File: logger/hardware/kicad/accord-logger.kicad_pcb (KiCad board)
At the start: 2 copper layers, 120 x 80 mm, 37 parts, among them J1 Board connector 14-way, J5 SD breakout 6-way, Q5 IPD50P04P4L-11, Q6 2N3904, Q7 2N3904, U1 RaspberryPi_Pico_W, U16 DS3231SN, U6 LM2678T-5.0

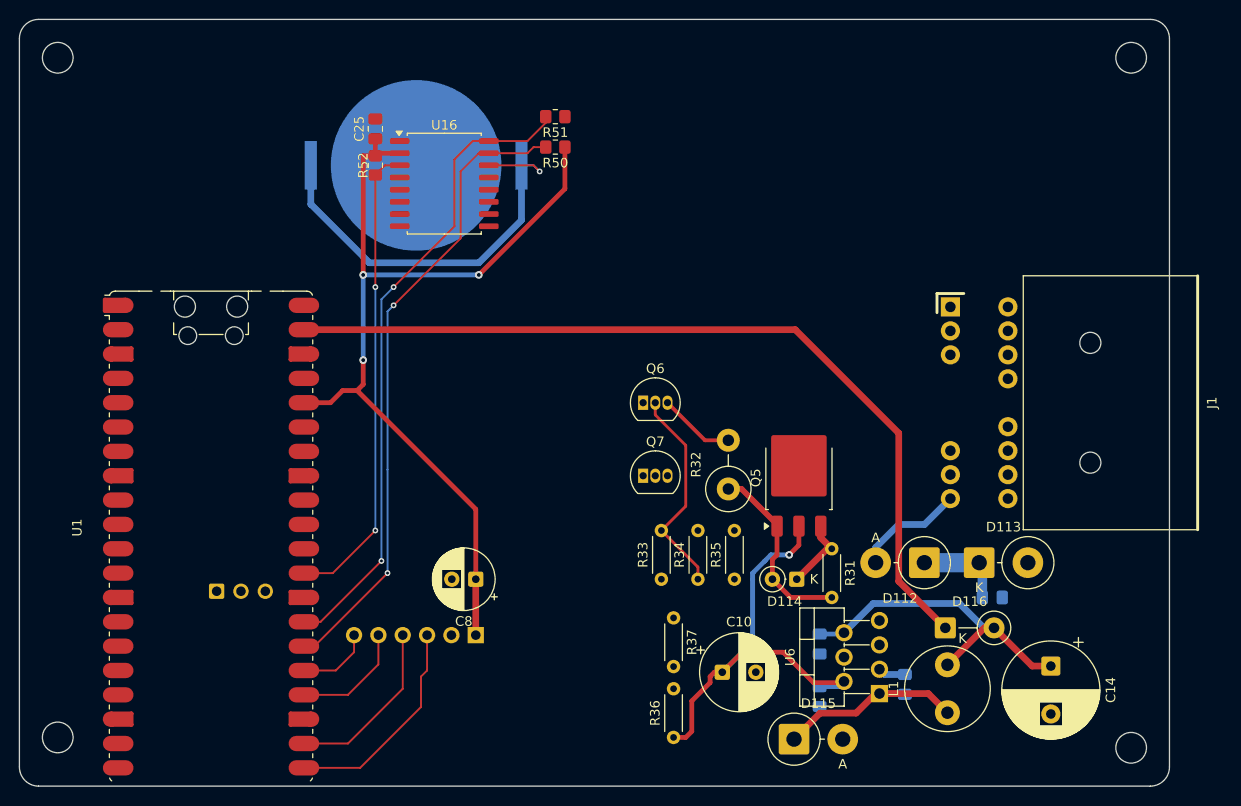
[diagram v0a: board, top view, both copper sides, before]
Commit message: layout: PGND pour on both layers; P12 and VIN_SW fixed
Owner revisions after review: P12 joined from D112 to Q5 pin 3
(15.8 mm); VIN_SW now lands on Q5's tab, not the middle lead; one PGND
zone on F.Cu and B.Cu, filled as a single island per layer, which joins
all 35 open ground connections. The Pico footprint's antenna and RF
keepouts already exclude it; the wider "suggestion" strip is to be cut
out later.

Open (scratch DRC, parity 0): starved thermal on U6 pin 4; C11 ground
pad reaches U6 pin 4 only through the back pour, around a VIN_SW stub;
unrouted R51.1 (3V3), R37.1 (B5), Q7.2-R35 (HOLD_B), U1.33-J1.10 (AGND,
with the inputs).

Claude-Session-ID: 42dd0e33-28b5-4936-847e-9c2e1d2488fa
Co-Authored-By: Claude Opus 5.5 <noreply@anthropic.com>
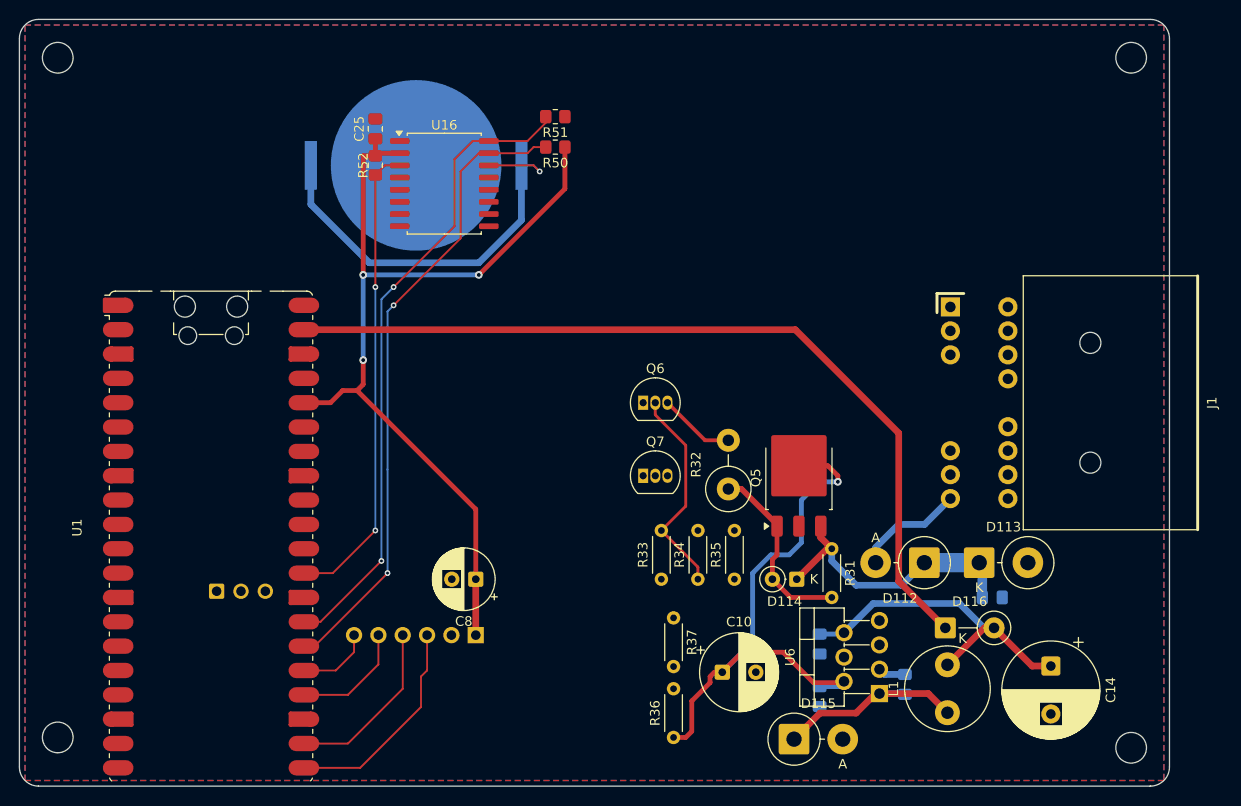
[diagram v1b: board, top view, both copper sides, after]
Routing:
- net /P12: track 17.3 -> 30.3 mm
- net /VIN_SW: track 47.5 -> 60.1 mm
- added copper zone on B.Cu, net /PGND
- added copper zone on F.Cu, net /PGND
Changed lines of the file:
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@@
+	)
+	(segment
+		(start 175.895 118.745)
+		(end 180.655 118.745)
+		(width 0.7)
+		(layer "B.Cu")
+		(net 6)
+	)
+	(segment
+		(start 173.355 114.935)
+		(end 173.355 116.205)
+		(width 0.7)
+		(layer "B.Cu")
+		(net 6)
+	)
+	(segment
+		(start 173.355 116.205)
+		(end 175.895 118.745)
+		(width 0.7)
+		(layer "B.Cu")
+		(net 6)
 	)
 	(segment
@@
 	)
 	(segment
+		(start 180.655 118.745)
+		(end 183.015 116.385)
+		(width 0.7)
+		(layer "B.Cu")
+		(net 6)
+	)
+	(segment
 		(start 183.015 116.385)
 		(end 188.735 116.385)
@@
 	)
 	(segment
-		(start 168.91 115.57)
-		(end 169.925 114.555)
+		(start 173.99 107.315)
+		(end 172.95 106.275)
 		(width 0.5)
 		(layer "F.Cu")
@@
 	)
 	(segment
+		(start 172.95 106.275)
+		(end 169.925 106.275)
+		(width 0.5)
+		(layer "F.Cu")
+		(net 7)
+	)
+	(segment
 		(start 168.275 125.73)
 		(end 171.45 128.905)
@@
 	)
 	(segment
-		(start 169.925 114.555)
-		(end 169.925 112.575)
-		(width 0.5)
-		(layer "F.Cu")
-		(net 7)
-	)
-	(segment
 		(start 158.75 133.985)
 		(end 158.75 130.81)
@@
 	)
 	(segment
+		(start 173.99 107.95)
+		(end 173.99 107.315)
+		(width 0.5)
+		(layer "F.Cu")
+		(net 7)
+	)
+	(segment
 		(start 171.45 128.905)
 		(end 174.499823 128.905)
@@
 	)
 	(via
-		(at 168.91 115.57)
+		(at 173.99 107.95)
 		(size 0.8)
 		(drill 0.4)
@@
 	)
 	(segment
+		(start 172.085 107.95)
+		(end 170.18 109.855)
+		(width 0.5)
+		(layer "B.Cu")
+		(net 7)
+	)
+	(segment
+		(start 165.1 124.645)
+		(end 161.93 127.815)
+		(width 0.5)
+		(layer "B.Cu")
+		(net 7)
+	)
+	(segment
+		(start 170.18 114.3)
+		(end 168.91 115.57)
+		(width 0.5)
+		(layer "B.Cu")
+		(net 7)
+	)
+	(segment
 		(start 167.005 115.57)
-		(end 168.91 115.57)
-		(width 0.5)
-		(layer "B.Cu")
-		(net 7)
-	)
-	(segment
-		(start 161.93 127.815)
-		(end 165.1 124.645)
+		(end 165.1 117.475)
 		(width 0.5)
 		(layer "B.Cu")
@@
 	)
 	(segment
+		(start 168.91 115.57)
+		(end 167.005 115.57)
+		(width 0.5)
+		(layer "B.Cu")
+		(net 7)
+	)
+	(segment
+		(start 173.99 107.95)
+		(end 172.085 107.95)
+		(width 0.5)
+		(layer "B.Cu")
+		(net 7)
+	)
+	(segment
+		(start 170.18 109.855)
+		(end 170.18 114.3)
+		(width 0.5)
+		(layer "B.Cu")
+		(net 7)
+	)
+	(segment
 		(start 174.087323 129.3175)
 		(end 174.63 128.774823)
@@
 	)
 	(segment
-		(start 166.37 116.205)
-		(end 167.005 115.57)
-		(width 0.5)
-		(layer "B.Cu")
-		(net 7)
-	)
-	(segment
-		(start 165.1 124.645)
-		(end 165.1 118.11)
-		(width 0.5)
-		(layer "B.Cu")
-		(net 7)
-	)
-	(segment
-		(start 165.1 118.11)
-		(end 165.1 117.475)
-		(width 0.5)
-		(layer "B.Cu")
-		(net 7)
-	)
-	(segment
 		(start 165.1 117.475)
-		(end 166.37 116.205)
+		(end 165.1 124.645)
 		(width 0.5)
 		(layer "B.Cu")
@@
 		(net 59)
 	)
+	(zone
+		(net 4)
+		(net_name "/PGND")
+		(layers "F.Cu" "B.Cu")
+		(hatch edge 0.5)
+		(connect_pads
+			(clearance 0.5)
+		)
+		(min_thickness 0.25)
+		(filled_areas_thickness no)
+		(fill yes
+			(thermal_gap 0.5)
+			(thermal_bridge_width 0.5)
+		)
+		(polygon
+			(pts
+				(xy 89.175787 60.285786) (xy 208.004214 60.285786) (xy 208.004214 139.114214) (xy 89.175787 139.114214)
+			)
+		)
+	)
 	(embedded_fonts no)

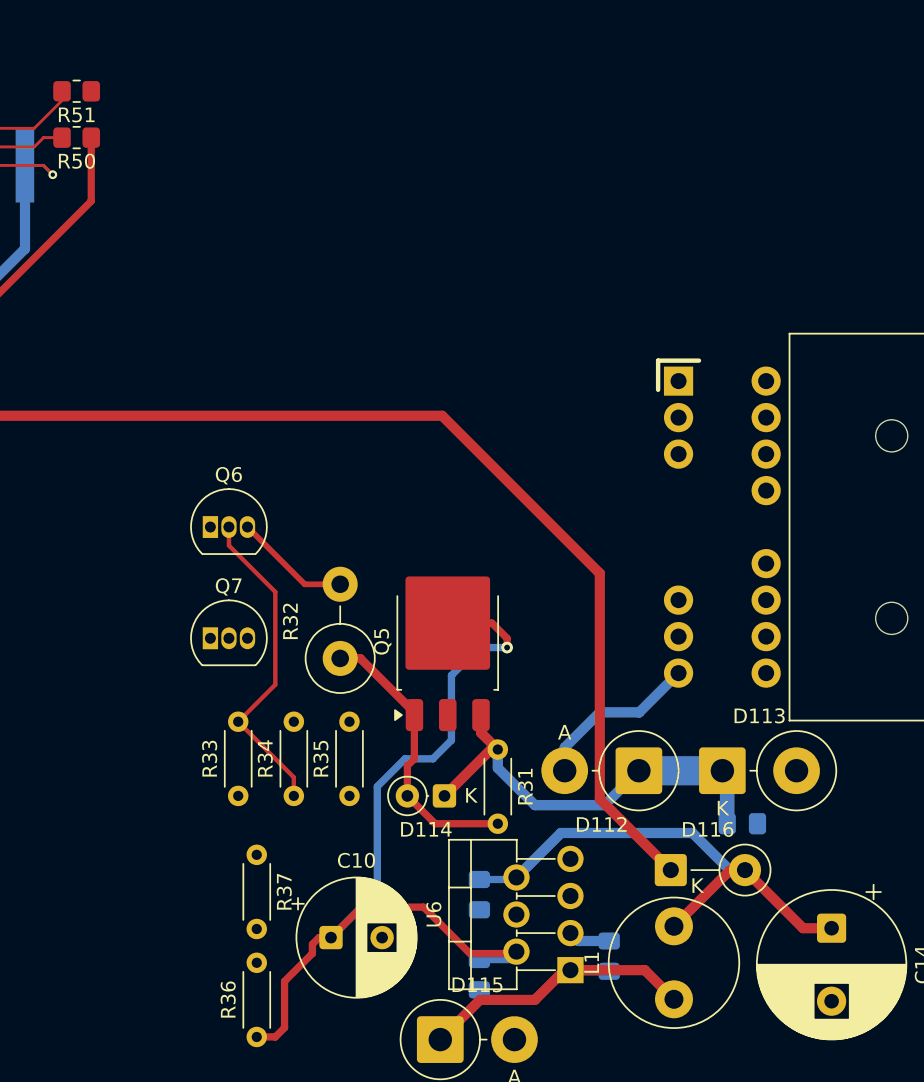
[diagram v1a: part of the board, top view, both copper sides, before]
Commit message: layout: remaining power-block connections routed
R51 pin 1 to 3V3 (3.2 mm to R50), Q7 base to R35 (HOLD_B, 15 mm,
0.2 mm B.Cu), R37 to B5; B5 rerouted at 0.5 mm; PGND tracks added at U6
pin 4 and C11 (C11 ground to U6.4 now 12.3 mm by track, plus the pour).

Saved with the PGND zone unfilled. Refilled in a scratch copy with the
pcbnew zone filler: one island per layer; DRC schematic parity 0, no
clearance, courtyard or thermal errors (the U6 pin 4 starved thermal is
gone); unconnected only U1.33-J1.10 (AGND, comes with the inputs) and
Q5's middle-lead pad (joined to the tab inside the part).

Claude-Session-ID: 42dd0e33-28b5-4936-847e-9c2e1d2488fa
Co-Authored-By: Claude Opus 5.5 <noreply@anthropic.com>
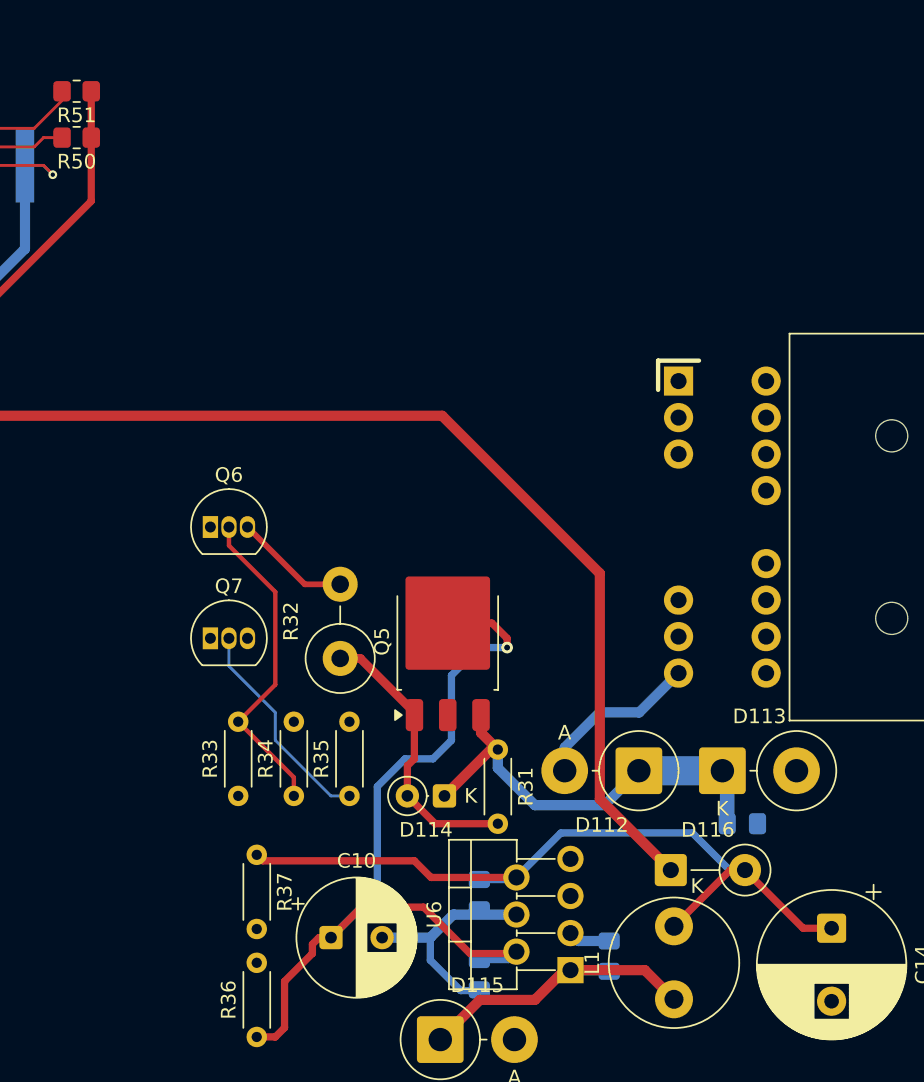
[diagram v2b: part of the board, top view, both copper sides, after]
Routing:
- net /B5: track 34.6 -> 53.0 mm
- net /PGND: track 0.00 -> 15.6 mm
- net /HOLD_B: track 0.00 -> 15.0 mm
- net /P3V3_SW: track 96.3 -> 99.5 mm
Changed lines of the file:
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@@
+	)
+	(segment
+		(start 170.815 131.445)
+		(end 168.73 129.36)
+		(width 0.5)
+		(layer "B.Cu")
+		(net 4)
+	)
+	(segment
+		(start 174.63 126.234823)
+		(end 170.310177 126.234823)
+		(width 0.7)
+		(layer "B.Cu")
+		(net 4)
+	)
+	(segment
+		(start 168.73 127.815)
+		(end 165.43 127.815)
+		(width 0.7)
+		(layer "B.Cu")
+		(net 4)
+	)
+	(segment
+		(start 168.73 129.36)
+		(end 168.73 127.815)
+		(width 0.5)
+		(layer "B.Cu")
+		(net 4)
+	)
+	(segment
+		(start 172.09 131.3925)
+		(end 172.0375 131.445)
+		(width 0.2)
+		(layer "B.Cu")
+		(net 4)
+	)
+	(segment
+		(start 170.310177 126.234823)
+		(end 168.73 127.815)
+		(width 0.7)
+		(layer "B.Cu")
+		(net 4)
+	)
+	(segment
+		(start 172.0375 131.445)
+		(end 170.815 131.445)
+		(width 0.5)
+		(layer "B.Cu")
+		(net 4)
 	)
 	(segment
@@
 		(end 136.2075 118.11)
 		(width 0.7)
+		(layer "F.Cu")
+		(net 5)
+	)
+	(segment
+		(start 145.51 73.025)
+		(end 145.51 69.85)
+		(width 0.5)
 		(layer "F.Cu")
 		(net 5)
@@
 		(start 196.215 127.172323)
 		(end 194.264506 127.172323)
-		(width 0.7)
+		(width 0.5)
 		(layer "F.Cu")
 		(net 10)
@@
 		(start 189.27 123.19)
 		(end 190.282183 123.19)
-		(width 0.7)
+		(width 0.5)
+		(layer "F.Cu")
+		(net 10)
+	)
+	(segment
+		(start 156.845 122.145)
+		(end 157.255 122.555)
+		(width 0.5)
 		(layer "F.Cu")
 		(net 10)
@@
 		(start 185.42 127.04)
 		(end 189.27 123.19)
-		(width 0.7)
+		(width 0.5)
+		(layer "F.Cu")
+		(net 10)
+	)
+	(segment
+		(start 157.255 122.555)
+		(end 167.64 122.555)
+		(width 0.5)
+		(layer "F.Cu")
+		(net 10)
+	)
+	(segment
+		(start 168.779823 123.694823)
+		(end 174.63 123.694823)
+		(width 0.5)
 		(layer "F.Cu")
 		(net 10)
@@
 		(start 194.264506 127.172323)
 		(end 190.282183 123.19)
-		(width 0.7)
+		(width 0.5)
+		(layer "F.Cu")
+		(net 10)
+	)
+	(segment
+		(start 167.64 122.555)
+		(end 168.779823 123.694823)
+		(width 0.5)
 		(layer "F.Cu")
 		(net 10)
@@
 		(start 174.63 123.694823)
 		(end 177.674823 120.65)
-		(width 0.7)
+		(width 0.5)
 		(layer "B.Cu")
 		(net 10)
@@
 		(start 186.69 120.65)
 		(end 189.23 123.19)
-		(width 0.7)
+		(width 0.5)
 		(layer "B.Cu")
 		(net 10)
@@
 		(start 189.23 123.19)
 		(end 190.282183 123.19)
-		(width 0.7)
+		(width 0.5)
 		(layer "B.Cu")
 		(net 10)
@@
 		(start 177.674823 120.65)
 		(end 186.69 120.65)
-		(width 0.7)
+		(width 0.5)
 		(layer "B.Cu")
 		(net 10)
@@
 		(layer "F.Cu")
 		(net 37)
+	)
+	(segment
+		(start 158.115 114.3)
+		(end 161.925 118.11)
+		(width 0.2)
+		(layer "B.Cu")
+		(net 39)
+	)
+	(segment
+		(start 158.115 112.395)
+		(end 158.115 114.3)
+		(width 0.2)
+		(layer "B.Cu")
+		(net 39)
+	)
+	(segment
+		(start 154.94 109.22)
+		(end 158.115 112.395)
+		(width 0.2)
+		(layer "B.Cu")
+		(net 39)
+	)
+	(segment
+		(start 161.925 118.11)
+		(end 163.195 118.11)
+		(width 0.2)
+		(layer "B.Cu")
+		(net 39)
+	)
+	(segment
+		(start 154.94 107.315)
+		(end 154.94 109.22)
+		(width 0.2)
+		(layer "B.Cu")
+		(net 39)
 	)
 	(segment
@@
 		(min_thickness 0.25)
 		(filled_areas_thickness no)
-		(fill yes
+		(fill
 			(thermal_gap 0.5)
 			(thermal_bridge_width 0.5)

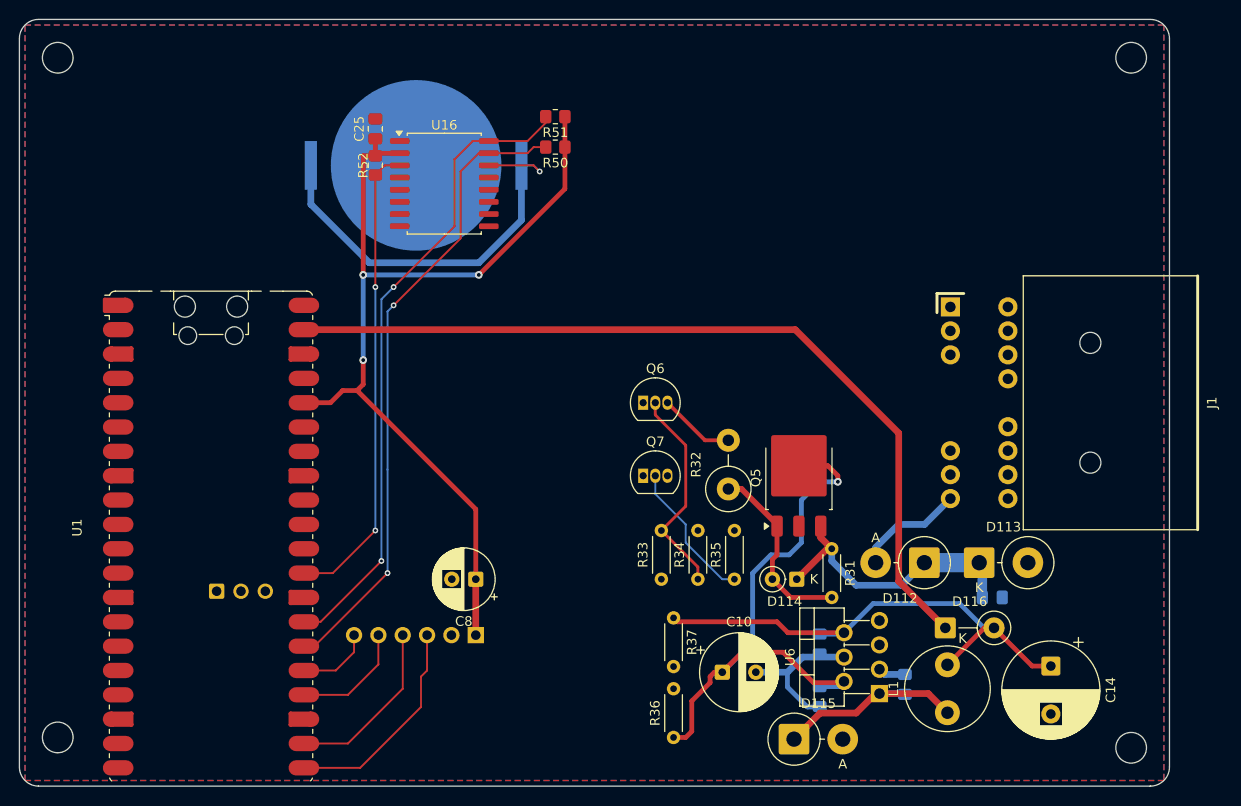
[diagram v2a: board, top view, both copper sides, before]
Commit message: layout: rs485 step placed and routed
Owner switched on the rs485 step (U15, C24, R30) and, after a first try
under the flush-mounted Pico, placed U15 (DIP-8 socket) between the Pico
and J1 at the top of the board with R30 3.5 mm from DE/RE and C24 4.9 mm
from VCC. A/B run 55 mm to J1.1/J1.7 as a 0.4 mm pair on B.Cu; GP8/GP9/
GP10 run 84-97 mm with four vias each. Everything is 40 mm or more from
the SW node.

Scratch copy refilled with the pcbnew zone filler: one PGND island per
layer; DRC schematic parity 0, no clearance or courtyard errors;
unconnected only U1.33-J1.10 (AGND, with the inputs) and Q5's
middle-lead pad (joined to the tab inside the part).

Claude-Session-ID: 42dd0e33-28b5-4936-847e-9c2e1d2488fa
Co-Authored-By: Claude Opus 5.5 <noreply@anthropic.com>
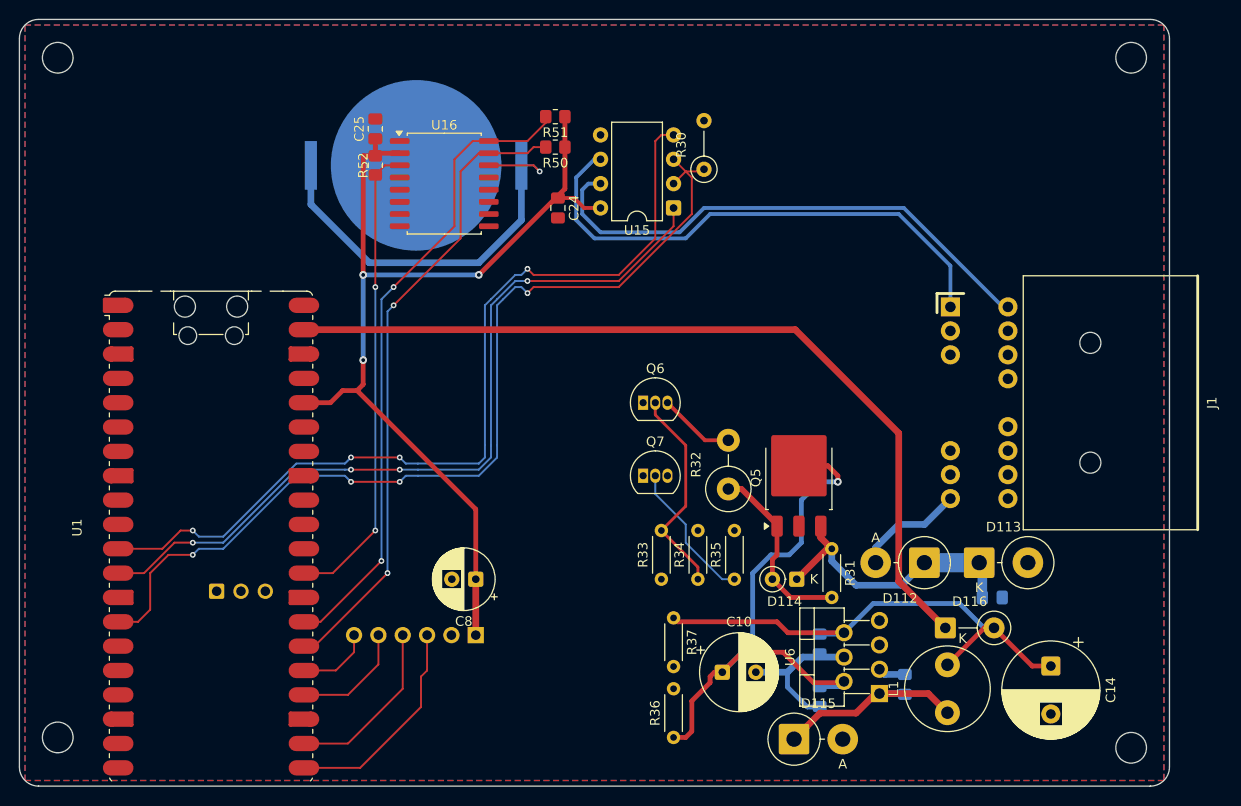
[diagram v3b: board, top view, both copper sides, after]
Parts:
- added C24: 100nF, Capacitor_SMD:C_0805_2012Metric_Pad1.18x1.45mm_HandSolder, F.Cu at (144.8, 79.4)
- added R30: 10k, Resistor_THT:R_Axial_DIN0207_L6.3mm_D2.5mm_P5.08mm_Vertical, F.Cu at (160.0, 75.3)
- added U15: MAX3485, Package_DIP:DIP-8_W7.62mm, F.Cu at (156.8, 79.4)
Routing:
- net /BUS_DE: track 0.00 -> 100.4 mm, vias 0 -> 4
- net /UART1_TX: track 0.00 -> 92.7 mm, vias 0 -> 4
- net /UART1_RX: track 0.00 -> 84.2 mm, vias 0 -> 4
- net /RS485_B: track 0.00 -> 55.2 mm
- net /RS485_A: track 0.00 -> 55.2 mm
- net /P3V3_SW: track 99.5 -> 104.3 mm
